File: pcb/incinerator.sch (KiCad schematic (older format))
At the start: 20 parts, among them J1 Furnace Control, J2 ESP32 NodeMCU, J3 ESP32 NodeMCU, J4 Waveshare 4.2\" e-paper, SW1 Rotary_Encoder_Switch

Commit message: Add low side MOSFETs for furnace control
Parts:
- removed D2, D3, D4, D5, D6, D7: LED, symbol Device:LED
- removed J1: Furnace Control, symbol Connector:Conn_01x06_Male
- added D1, D2, D3, D4, D5, D6: D, symbol Device:D
- added J1: IGNITION1, symbol Connector:Screw_Terminal_01x02
- added J2: IGNITION2, symbol Connector:Screw_Terminal_01x02
- added J3: VALVE1, symbol Connector:Screw_Terminal_01x02
- added J4: VALVE2, symbol Connector:Screw_Terminal_01x02
- added J5: VALVE3, symbol Connector:Screw_Terminal_01x02
- added J6: AIRPMP, symbol Connector:Screw_Terminal_01x02
- added J7: Power Source 12V, symbol Connector:Screw_Terminal_01x02
- added Q1, Q2, Q3, Q4, Q5, Q6: IRLU120N, symbol Device:Q_NMOS_GDS
- added R1, R2: 15k, symbol Device:R
- added R10, R11, R12, R9: 100, symbol Device:R
- added U1: R-78E9.0-0.5, Converter_DCDC:Converter_DCDC_RECOM_R-78E-0.5_THT, symbol Regulator_Switching:R-78E9.0-0.5
- R3, R4, R5, R6: value 50 -> 15k
- R7, R8: value 50 -> 100
- gave numbers to parts that had none: 2
- renumbered J4 to J10, J2 to J8, J3 to J9
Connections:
- net labels added: +12V
- net labels removed: AIRPMP, IGNITION1, IGNITION2, VALVE1, VALVE2, VALVE3
- wire segments 82 -> 177
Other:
- moved on the sheet: BZ1, J10, J11, J12, J8, J9, SW1

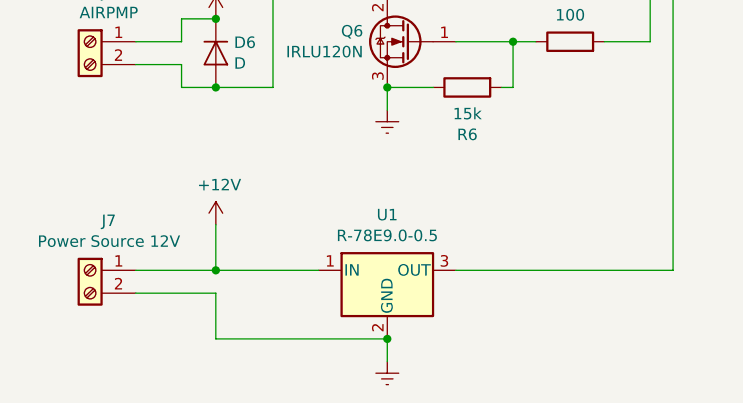
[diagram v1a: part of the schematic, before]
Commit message: Update DCDC info & added support capacitor
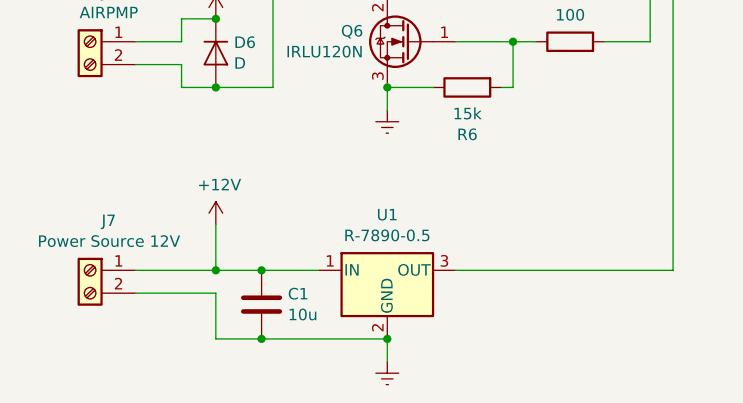
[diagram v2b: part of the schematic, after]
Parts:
- added C1: 10u, symbol Device:C
- U1: value R-78E9.0-0.5 -> R-7890-0.5
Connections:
- net +12V: now also C1.1
- net Earth: now also C1.2
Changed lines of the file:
@@
 P 2450 6050
 F 0 "U1" H 2450 6292 50  0000 C CNN
-F 1 "R-78E9.0-0.5" H 2450 6201 50  0000 C CNN
+F 1 "R-7890-0.5" H 2450 6201 50  0000 C CNN
 F 2 "Converter_DCDC:Converter_DCDC_RECOM_R-78E-0.5_THT" H 2500 5800 50  0001 L CIN
-F 3 "https://www.recom-power.com/pdf/Innoline/R-78Exx-0.5.pdf" H 2450 6050 50  0001 C CNN
+F 3 "https://cdn-reichelt.de/documents/datenblatt/D400/R-78XX-05.pdf" H 2450 6050 50  0001 C CNN
 	1    2450 6050
 	1    0    0    -1
@@
 Connection ~ 1700 6050
 Wire Wire Line
-	1700 6050 2150 6050
+	1700 6050 1900 6050
 Wire Wire Line
 	1700 6150 1700 6350
 Wire Wire Line
-	1700 6350 2450 6350
+	1700 6350 1900 6350
 Wire Wire Line
 	2450 6450 2450 6350
@@
 Wire Wire Line
 	6750 4450 6400 4450
+$Comp
+L Device:C C1
+U 1 1 5E12B8A7
+P 1900 6200
+F 0 "C1" H 2015 6246 50  0000 L CNN
+F 1 "10u" H 2015 6155 50  0000 L CNN
+F 2 "" H 1938 6050 50  0001 C CNN
+F 3 "~" H 1900 6200 50  0001 C CNN
+	1    1900 6200
+	1    0    0    -1
+$EndComp
+Connection ~ 1900 6050
+Wire Wire Line
+	1900 6050 2150 6050
+Connection ~ 1900 6350
+Wire Wire Line
+	1900 6350 2450 6350
 $EndSCHEMATC

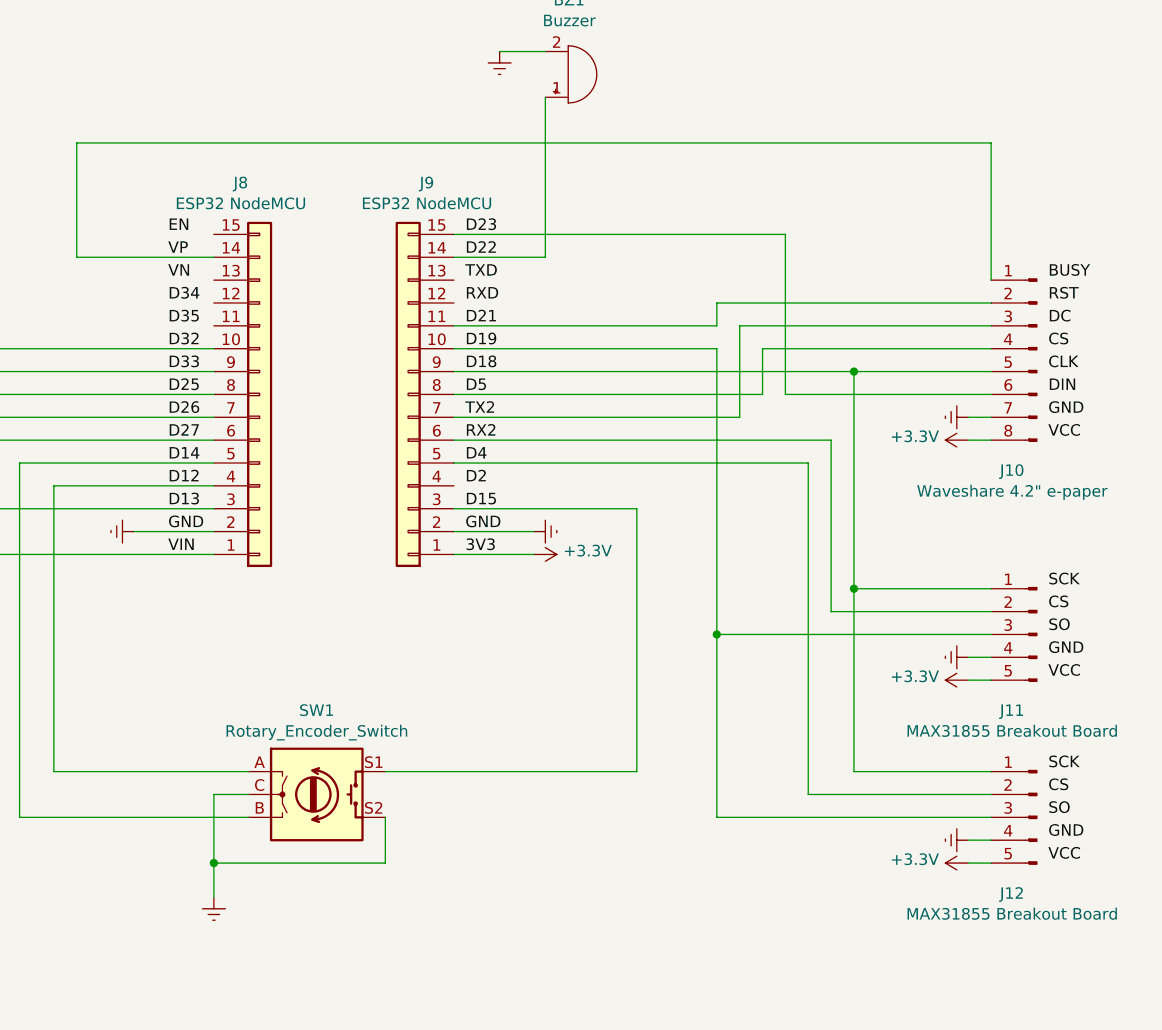
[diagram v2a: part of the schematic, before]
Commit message: Added project-specific KiCad library for breakout boards
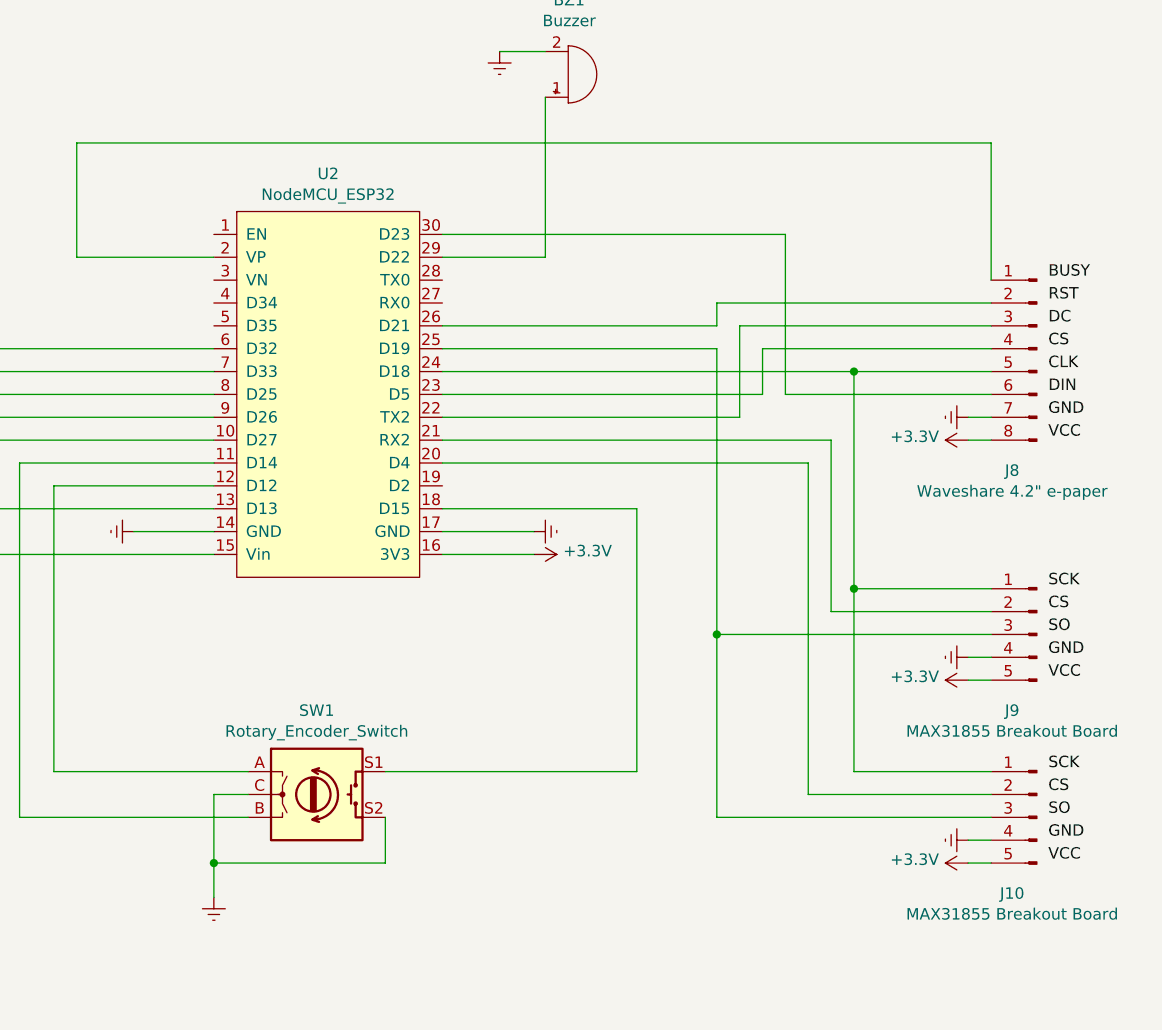
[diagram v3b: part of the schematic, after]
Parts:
- removed J8, J9: ESP32 NodeMCU, symbol Connector_Generic:Conn_01x15
- added U2: NodeMCU_ESP32, symbol incinerator:NodeMCU_ESP32
- renumbered J12 to J10, J10 to J8, J11 to J9
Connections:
- net +3V3: now also U2.16 (3V3)
- net Earth: now also U2.14 (GND), U2.17 (GND)
- net D12: no longer names the net of SW1.A
- net D12: now also U2.12 (D12)
- net D13: no longer names the net of R12.2
- net D13: now also U2.13 (D13)
- net D14: no longer names the net of SW1.B
- net D14: now also U2.11 (D14)
- net D15: no longer names the net of SW1.S1
- net D15: now also U2.18 (D15)
- net D18: no longer names the net of J10.1 (Pin_1), J8.5 (Pin_5), J9.1 (Pin_1)
- net D18: now also U2.24 (D18)
- net D19: no longer names the net of J10.3 (Pin_3), J9.3 (Pin_3)
- net D19: now also U2.25 (D19)
- net D21: no longer names the net of J8.2 (Pin_2)
- net D21: now also U2.26 (D21)
- net D22: no longer names the net of BZ1.1 (-)
- net D22: now also U2.29 (D22)
- net D23: no longer names the net of J8.6 (Pin_6)
- net D23: now also U2.30 (D23)
- net D25: no longer names the net of R9.2
- net D25: now also U2.8 (D25)
- net D26: no longer names the net of R10.2
- net D26: now also U2.9 (D26)
- net D27: no longer names the net of R11.2
- net D27: now also U2.10 (D27)
- net D32: no longer names the net of R7.2
- net D32: now also U2.6 (D32)
- net D33: no longer names the net of R8.2
- net D33: now also U2.7 (D33)
- net D4: no longer names the net of J10.2 (Pin_2)
- net D4: now also U2.20 (D4)
- net D5: no longer names the net of J8.4 (Pin_4)
- net D5: now also U2.23 (D5)
- net RX2: no longer names the net of J9.2 (Pin_2)
- net RX2: now also U2.21 (RX2)
- net TX2: no longer names the net of J8.3 (Pin_3)
- net TX2: now also U2.22 (TX2)
- net VIN: no longer names the net of U1.3 (OUT)
- net VIN: now also U2.15 (Vin)
- net VP: no longer names the net of J8.1 (Pin_1)
- net VP: now also U2.2 (VP)
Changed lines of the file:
@@
 Wire Wire Line
 	8200 3250 8200 2550
-Wire Wire Line
-	7800 3250 8200 3250
 $Comp
 L Device:Buzzer BZ1
@@
 	8950 3550 8950 3450
 Wire Wire Line
-	7800 3550 8950 3550
-Wire Wire Line
 	9150 3850 9150 3650
 Wire Wire Line
-	7800 3850 9150 3850
-Wire Wire Line
 	6150 2750 6150 3250
 Wire Wire Line
 	10150 2750 6150 2750
-Wire Wire Line
-	7800 3150 9250 3150
-Text Label 7850 4550 0    50   ~ 0
-3V3
-Text Label 7850 4450 0    50   ~ 0
-GND
-Text Label 7850 4350 0    50   ~ 0
-D15
-Text Label 7850 4250 0    50   ~ 0
-D2
-Text Label 7850 3950 0    50   ~ 0
-TX2
-Text Label 7850 3850 0    50   ~ 0
-D5
-Text Label 7850 3750 0    50   ~ 0
-D18
-Text Label 7850 3650 0    50   ~ 0
-D19
-Text Label 7850 3550 0    50   ~ 0
-D21
-Text Label 7850 3450 0    50   ~ 0
-RXD
-Text Label 7850 3350 0    50   ~ 0
-TXD
-Text Label 7850 3250 0    50   ~ 0
-D22
-Text Label 7850 3150 0    50   ~ 0
-D23
-Text Label 6550 4550 0    50   ~ 0
-VIN
-Text Label 6550 4450 0    50   ~ 0
-GND
-Text Label 6550 4350 0    50   ~ 0
-D13
-Text Label 6550 4250 0    50   ~ 0
-D12
-Text Label 6550 4150 0    50   ~ 0
-D14
-Text Label 6550 4050 0    50   ~ 0
-D27
-Text Label 6550 3950 0    50   ~ 0
-D26
-Text Label 6550 3850 0    50   ~ 0
-D25
-Text Label 6550 3750 0    50   ~ 0
-D33
-Text Label 6550 3650 0    50   ~ 0
-D32
-Text Label 6550 3550 0    50   ~ 0
-D35
-Text Label 6550 3450 0    50   ~ 0
-D34
-Text Label 6550 3350 0    50   ~ 0
-VN
-Text Label 6550 3250 0    50   ~ 0
-VP
-Text Label 6550 3150 0    50   ~ 0
-EN
-$Comp
-L Connector_Generic:Conn_01x15 J9
-U 1 1 5DD97FE0
-P 7600 3850
-F 0 "J9" H 7518 2925 50  0000 C CNN
-F 1 "ESP32 NodeMCU" H 7518 3016 50  0000 C CNN
-F 2 "" H 7600 3850 50  0001 C CNN
-F 3 "~" H 7600 3850 50  0001 C CNN
-	1    7600 3850
-	-1   0    0    1
-$EndComp
-$Comp
-L Connector_Generic:Conn_01x15 J8
-U 1 1 5DD971B9
-P 6950 3850
-F 0 "J8" H 6868 2925 50  0000 C CNN
-F 1 "ESP32 NodeMCU" H 6868 3016 50  0000 C CNN
-F 2 "" H 6950 3850 50  0001 C CNN
-F 3 "~" H 6950 3850 50  0001 C CNN
-	1    6950 3850
-	1    0    0    1
-$EndComp
-Wire Wire Line
-	9050 3950 7800 3950
 Wire Wire Line
 	9050 3550 9050 3950
@@
 Wire Wire Line
 	6900 5700 5900 5700
-Wire Wire Line
-	7800 3750 9550 3750
 Text Label 10400 5100 0    50   ~ 0
 VCC
@@
 SCK
 $Comp
-L Connector:Conn_01x05_Male J11
+L Connector:Conn_01x05_Male J9
 U 1 1 5DE8FF2A
 P 10350 4900
-F 0 "J11" H 10458 4567 50  0000 C CNN
+F 0 "J9" H 10458 4567 50  0000 C CNN
 F 1 "MAX31855 Breakout Board" H 10458 4476 50  0000 C CNN
 F 2 "" H 10350 4900 50  0001 C CNN
@@
 SCK
 $Comp
-L Connector:Conn_01x05_Male J12
+L Connector:Conn_01x05_Male J10
 U 1 1 5DEAED10
 P 10350 5700
-F 0 "J12" H 10458 5367 50  0000 C CNN
+F 0 "J10" H 10458 5367 50  0000 C CNN
 F 1 "MAX31855 Breakout Board" H 10458 5276 50  0000 C CNN
 F 2 "" H 10350 5700 50  0001 C CNN
@@
 Wire Wire Line
 	9450 4800 10150 4800
-Text Label 7850 4050 0    50   ~ 0
-RX2
-Text Label 7850 4150 0    50   ~ 0
-D4
-Wire Wire Line
-	7800 4050 9450 4050
 Wire Wire Line
 	9450 4050 9450 4800
 Wire Wire Line
-	7800 4150 9350 4150
-Wire Wire Line
 	9350 4150 9350 5600
 Wire Wire Line
@@
 Wire Wire Line
 	9250 3150 9250 3850
-Wire Wire Line
-	7800 3650 8950 3650
 Wire Wire Line
 	8950 3650 8950 4900
@@
 	10050 3950 10150 3950
 $Comp
-L Connector:Conn_01x08_Male J10
+L Connector:Conn_01x08_Male J8
 U 1 1 5DDAE1A1
 P 10350 3650
-F 0 "J10" H 10458 3117 50  0000 C CNN
+F 0 "J8" H 10458 3117 50  0000 C CNN
 F 1 "Waveshare 4.2\" e-paper" H 10458 3026 50  0000 C CNN
 F 2 "" H 10350 3650 50  0001 C CNN
@@
 	8600 4350 8600 5500
 Wire Wire Line
-	7800 4350 8600 4350
-Wire Wire Line
 	7500 5500 8600 5500
 $Comp
@@
 $EndComp
 Wire Wire Line
-	7800 4450 8150 4450
-Wire Wire Line
-	7800 4550 8150 4550
-Wire Wire Line
 	6750 4250 6050 4250
 Wire Wire Line
@@
 Wire Wire Line
 	1900 6350 2450 6350
+$Comp
+L incinerator:NodeMCU_ESP32 U2
+U 1 1 5E143B46
+P 7250 3900
+F 0 "U2" H 7250 4915 50  0000 C CNN
+F 1 "NodeMCU_ESP32" H 7250 4824 50  0000 C CNN
+F 2 "" H 7100 4200 50  0001 C CNN
+F 3 "" H 7100 4200 50  0001 C CNN
+	1    7250 3900
+	1    0    0    -1
+$EndComp
+Wire Wire Line
+	7750 3150 9250 3150
+Wire Wire Line
+	7750 3250 8200 3250
+Wire Wire Line
+	7750 3550 8950 3550
+Wire Wire Line
+	7750 3650 8950 3650
+Wire Wire Line
+	7750 3750 9550 3750
+Wire Wire Line
+	7750 3850 9150 3850
+Wire Wire Line
+	7750 3950 9050 3950
+Wire Wire Line
+	7750 4050 9450 4050
+Wire Wire Line
+	7750 4150 9350 4150
+Wire Wire Line
+	7750 4350 8600 4350
+Wire Wire Line
+	7750 4450 8150 4450
+Wire Wire Line
+	7750 4550 8150 4550
 $EndSCHEMATC
